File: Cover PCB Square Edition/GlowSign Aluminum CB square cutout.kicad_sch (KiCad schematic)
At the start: 10 parts, among them U1 SMTSO3030CTJ, U2 SMTSO3030CTJ, U3 SMTSO3030CTJ, U4 SMTSO3030CTJ

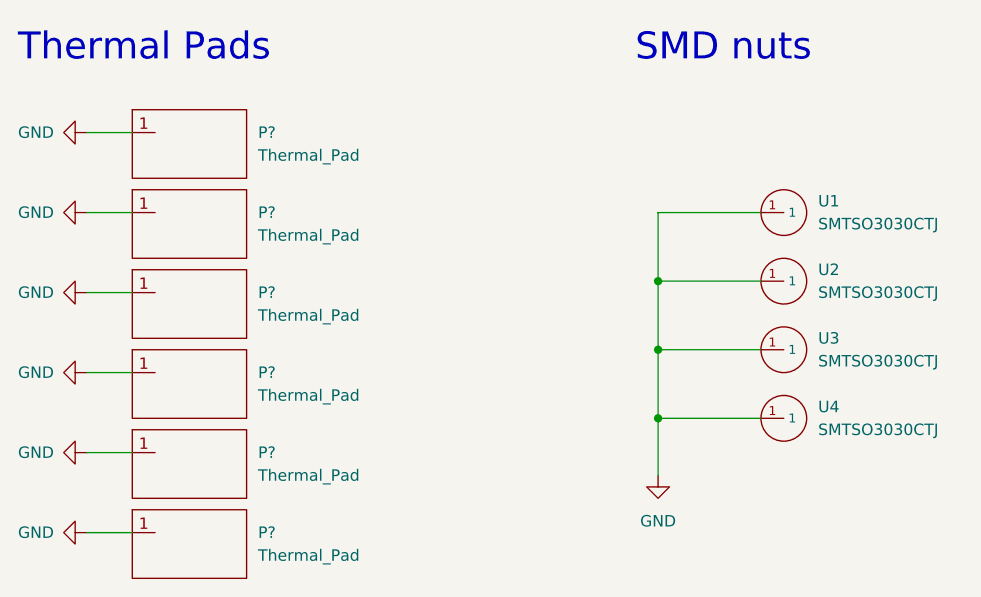
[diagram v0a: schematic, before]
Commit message: updated cover circle pcb
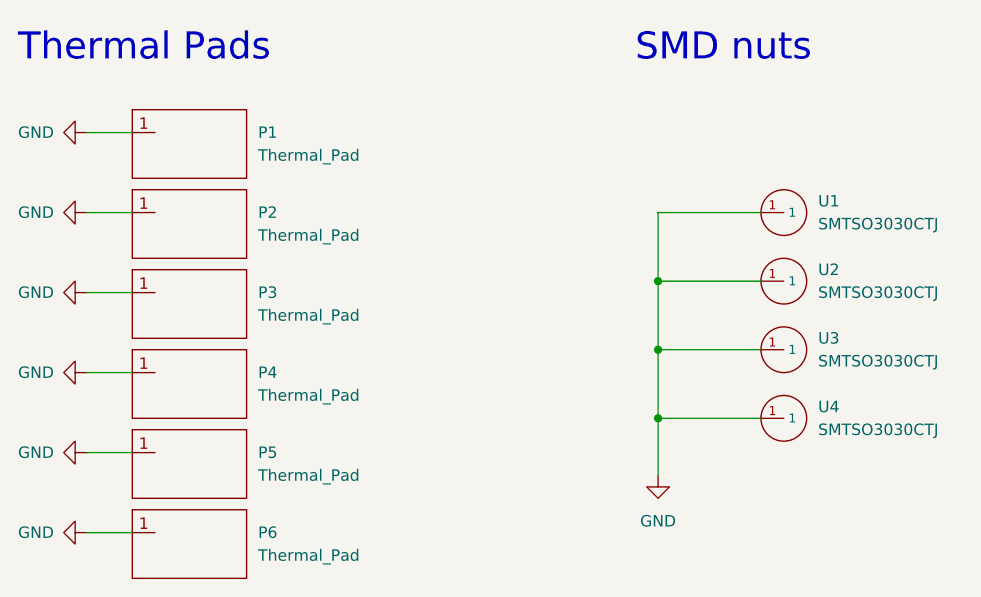
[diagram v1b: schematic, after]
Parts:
- gave numbers to parts that had none: 6
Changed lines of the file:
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@@
   (symbol (lib_id "MyParts:Thermal_Pad") (at 38.1 68.58 0) (unit 1)
     (in_bom no) (on_board yes) (fields_autoplaced)
-    (property "Reference" "P?" (id 0) (at 52.07 68.5799 0)
+    (property "Reference" "P4" (id 0) (at 52.07 68.5799 0)
       (effects (font (size 1.27 1.27)) (justify left))
     )
@@
   (symbol (lib_id "MyParts:Thermal_Pad") (at 38.1 50.8 0) (unit 1)
     (in_bom no) (on_board yes) (fields_autoplaced)
-    (property "Reference" "P?" (id 0) (at 52.07 50.7999 0)
+    (property "Reference" "P2" (id 0) (at 52.07 50.7999 0)
       (effects (font (size 1.27 1.27)) (justify left))
     )
@@
   (symbol (lib_id "MyParts:Thermal_Pad") (at 38.1 86.36 0) (unit 1)
     (in_bom no) (on_board yes) (fields_autoplaced)
-    (property "Reference" "P?" (id 0) (at 52.07 86.3599 0)
+    (property "Reference" "P6" (id 0) (at 52.07 86.3599 0)
       (effects (font (size 1.27 1.27)) (justify left))
     )
@@
   (symbol (lib_id "MyParts:Thermal_Pad") (at 38.1 77.47 0) (unit 1)
     (in_bom no) (on_board yes) (fields_autoplaced)
-    (property "Reference" "P?" (id 0) (at 52.07 77.4699 0)
+    (property "Reference" "P5" (id 0) (at 52.07 77.4699 0)
       (effects (font (size 1.27 1.27)) (justify left))
     )
@@
   (symbol (lib_id "MyParts:Thermal_Pad") (at 38.1 41.91 0) (unit 1)
     (in_bom no) (on_board yes) (fields_autoplaced)
-    (property "Reference" "P?" (id 0) (at 52.07 41.9099 0)
+    (property "Reference" "P1" (id 0) (at 52.07 41.9099 0)
       (effects (font (size 1.27 1.27)) (justify left))
     )
@@
   (symbol (lib_id "MyParts:Thermal_Pad") (at 38.1 59.69 0) (unit 1)
     (in_bom no) (on_board yes) (fields_autoplaced)
-    (property "Reference" "P?" (id 0) (at 52.07 59.6899 0)
+    (property "Reference" "P3" (id 0) (at 52.07 59.6899 0)
       (effects (font (size 1.27 1.27)) (justify left))
     )
@@
       (reference "#PWR?") (unit 1) (value "GND") (footprint "")
     )
+    (path "/e771895d-f993-4350-b292-891afbb550d8"
+      (reference "P1") (unit 1) (value "Thermal_Pad") (footprint "footprint:Thermal pad")
+    )
+    (path "/6fa05cd5-065e-465f-b08d-7ecbf9d2acc3"
+      (reference "P2") (unit 1) (value "Thermal_Pad") (footprint "footprint:Thermal pad")
+    )
+    (path "/f0908454-8649-4133-a848-f2c0631cb9af"
+      (reference "P3") (unit 1) (value "Thermal_Pad") (footprint "footprint:Thermal pad")
+    )
     (path "/3ab2c8aa-3b10-430e-b61d-ea401f58f6e6"
-      (reference "P?") (unit 1) (value "Thermal_Pad") (footprint "footprint:Thermal pad")
-    )
-    (path "/6fa05cd5-065e-465f-b08d-7ecbf9d2acc3"
-      (reference "P?") (unit 1) (value "Thermal_Pad") (footprint "footprint:Thermal pad")
+      (reference "P4") (unit 1) (value "Thermal_Pad") (footprint "footprint:Thermal pad")
+    )
+    (path "/d707b9a9-5a70-4e84-9567-d6bec7a50599"
+      (reference "P5") (unit 1) (value "Thermal_Pad") (footprint "footprint:Thermal pad")
     )
     (path "/897f42df-a867-4b46-b04e-9979b57053bd"
-      (reference "P?") (unit 1) (value "Thermal_Pad") (footprint "footprint:Thermal pad")
-    )
-    (path "/d707b9a9-5a70-4e84-9567-d6bec7a50599"
-      (reference "P?") (unit 1) (value "Thermal_Pad") (footprint "footprint:Thermal pad")
-    )
-    (path "/e771895d-f993-4350-b292-891afbb550d8"
-      (reference "P?") (unit 1) (value "Thermal_Pad") (footprint "footprint:Thermal pad")
-    )
-    (path "/f0908454-8649-4133-a848-f2c0631cb9af"
-      (reference "P?") (unit 1) (value "Thermal_Pad") (footprint "footprint:Thermal pad")
+      (reference "P6") (unit 1) (value "Thermal_Pad") (footprint "footprint:Thermal pad")
     )
     (path "/65bd98ca-4fd6-454c-92d4-f797652e0f9e"

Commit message: separated battery electronics into separate pcb
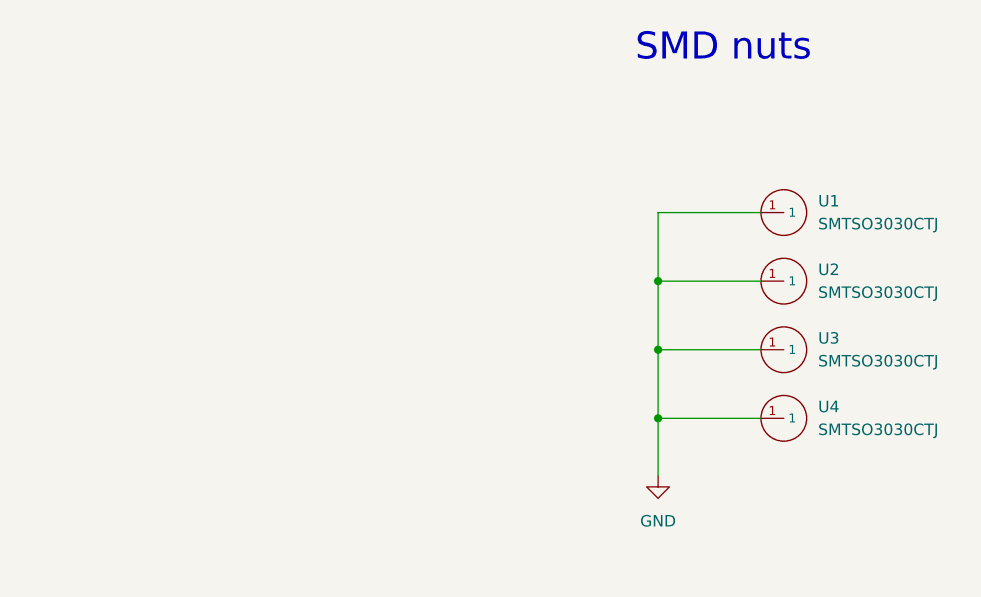
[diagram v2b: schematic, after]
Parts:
- removed P1, P2, P3, P4, P5, P6: Thermal_Pad, footprint:Thermal pad, symbol MyParts:Thermal_Pad
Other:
- note removed: "Thermal Pads"
